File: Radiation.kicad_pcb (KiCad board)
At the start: 4 copper layers, 102 x 125 mm, 114 parts, among them J1 USB4105-GF-A, J2 USB4105-GF-A, J3 AUDIO JACK, J4 MEM2061-01-188-00-A, J5 1x6 header, Q1 AO3400A, Q2 2N7002-TP, Q3 2N7002-TP, Q4 BC846, T1 FL2810-1L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

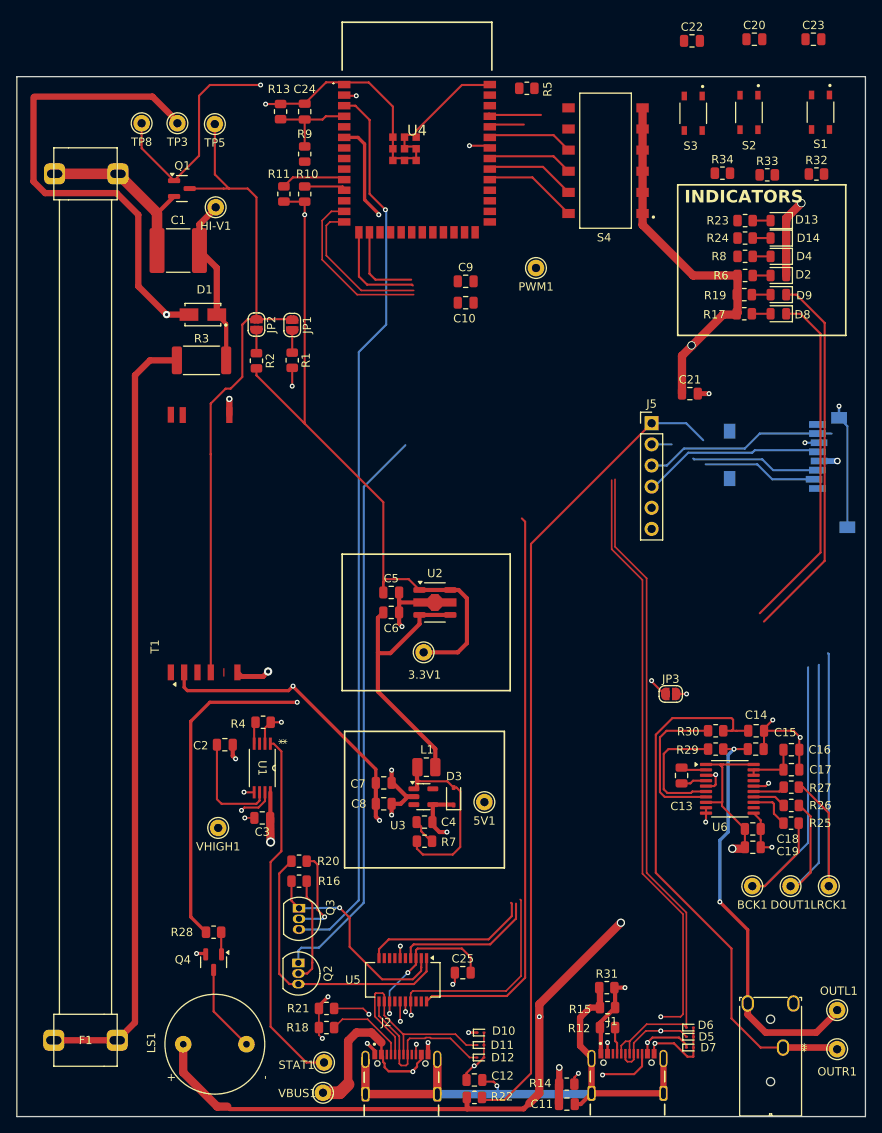
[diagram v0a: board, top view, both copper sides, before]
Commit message: Updated schematics/ pcb
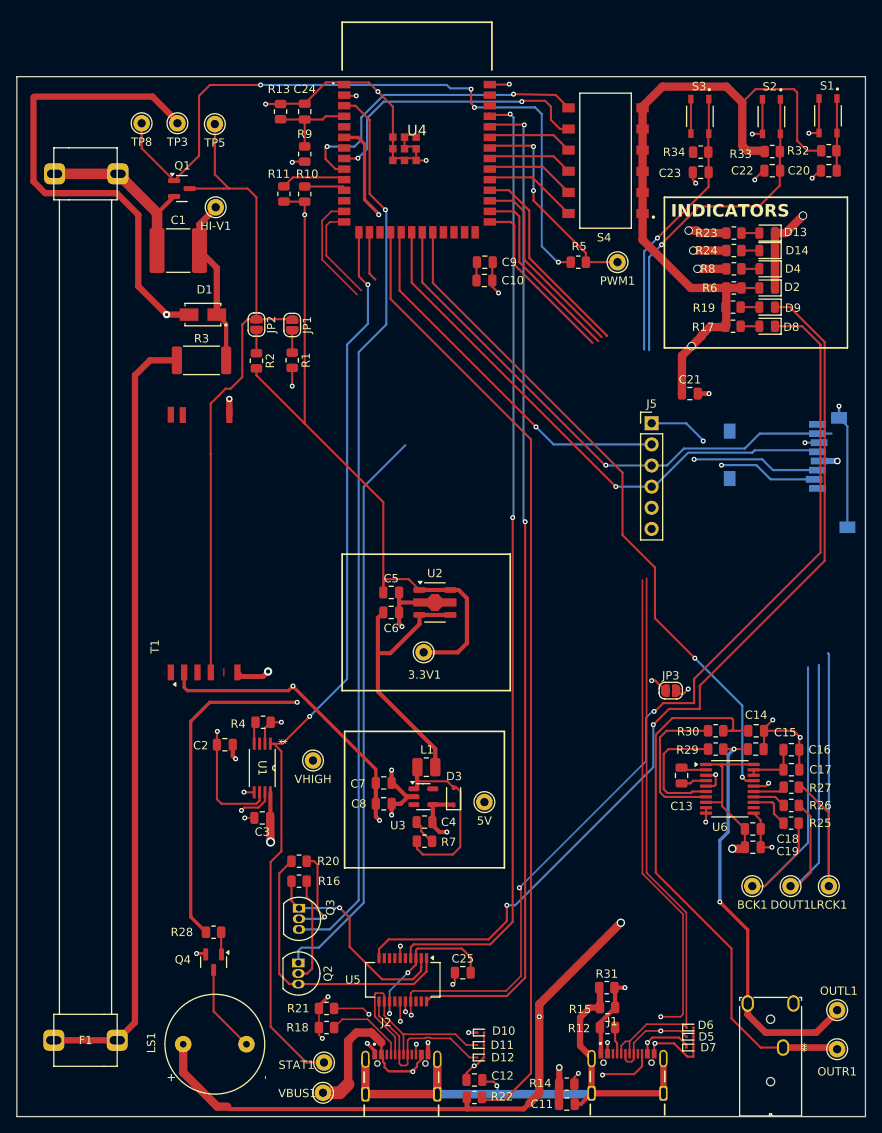
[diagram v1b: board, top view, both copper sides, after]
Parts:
- moved R5 21.8 mm to (104.7, 84.2), turned to 0 degrees
- moved C23 21.0 mm to (119.4, 73.4)
- moved C22 18.3 mm to (128.0, 73.2)
- moved C20 18.2 mm to (134.8, 73.2)
- moved VHIGH 14.0 mm to (72.8, 144.1)
- moved PWM1 9.82 mm to (109.4, 84.2)
- moved R34 3.64 mm to (119.4, 71.0), turned to 180 degrees
- moved C10 3.49 mm to (93.4, 86.4)
- moved C9 3.25 mm to (93.5, 84.2)
- moved R32 3.17 mm to (134.8, 70.8), turned to 180 degrees
- moved R33 2.86 mm to (128.0, 70.9), turned to 180 degrees
- moved S2 2.75 mm to (127.9, 66.7)
- moved D13 2.02 mm to (127.4, 80.7)
- moved D14 2.02 mm to (127.4, 82.8)
- moved D2 2.02 mm to (127.4, 87.3)
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- renumbered 5V1 to 5V, VHIGH1 to VHIGH
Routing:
- net VBUS: track 103.2 -> 213.6 mm, vias 5 -> 6
- net /MCU/TX: track 23.5 -> 115.0 mm, vias 0 -> 2
- net +VBAT: track 13.1 -> 98.0 mm, vias 0 -> 3
- net /MUTE: track 0.00 -> 82.4 mm, vias 0 -> 2
- net +3.3V: track 313.0 -> 377.3 mm
- net GND: track 348.0 -> 409.3 mm, vias 26 -> 35
- net /VSTAT: track 56.1 -> 111.0 mm, vias 0 -> 2
- net /MCU/RX_LED: track 67.8 -> 116.9 mm, vias 1 -> 3
- net /MOSI: track 17.9 -> 66.6 mm, vias 0 -> 2
- net /MCU/TX_LED: track 65.3 -> 113.7 mm, vias 0 -> 2
- net /MCU/RX: track 72.5 -> 119.9 mm, vias 0 -> 2
- net /SCK: track 21.8 -> 67.2 mm, vias 0 -> 1
- net /MISO: track 23.2 -> 65.8 mm, vias 0 -> 1
- net /EN: track 108.1 -> 149.1 mm, vias 1 -> 2
- net Net-(Q1-G): track 45.7 -> 84.9 mm, vias 1 -> 4
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- added copper zone on In2.Cu, net +500V

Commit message: revisions after design review by Ted Yapo
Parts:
- removed 5V, VHIGH: TestPoint, Connector_Pin:Pin_D1.0mm_L10.0mm
- added 5V1: TestPoint, Connector_Pin:Pin_D1.0mm_L10.0mm, F.Cu at (93.5, 148.9)
- added C26: 2.2uF, Capacitor_SMD:C_0805_2012Metric, F.Cu at (118.7, 152.8)
- added VHIGH1: TestPoint, Connector_Pin:Pin_D1.0mm_L10.0mm, F.Cu at (93.4, 131.7)
- moved R27 78.8 mm to (97.9, 75.5), turned to 180 degrees
- moved R26 77.9 mm to (99.8, 77.8), turned to 180 degrees
- moved R25 77.8 mm to (99.9, 80.0), turned to 180 degrees
- moved LRCK1 11.2 mm to (135.3, 148.0)
- moved BCK1 10.3 mm to (135.3, 155.8)
- moved DOUT1 8.77 mm to (135.2, 152.0)
- moved OUTL1 4.70 mm to (135.8, 178.8)
- moved OUTR1 4.70 mm to (135.8, 174.1)
- moved R9 3.10 mm to (68.9, 70.1)
- moved S4 1.23 mm to (108.8, 71.1)
- moved C10 1.13 mm to (93.2, 87.5)
- moved C9 1.13 mm to (93.2, 85.3)
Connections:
- C16 pad 1: Net-(U6-DGND) -> Net-(U6-LDOO)
- C17 pad 1: Net-(U6-DGND) -> Net-(U6-LDOO)
- J3 pad 1: /Audio/OUTR -> AGND
- J3 pad 3: AGND -> /Audio/OUTR
- R25 pad 1: Net-(U6-BCK) -> /I2S_BCK
- R25 pad 2: /I2S_BCK -> Net-(U4-IO35)
- R26 pad 1: Net-(U6-DIN) -> /I2S_LRCK
- R26 pad 2: /I2S_DOUT -> Net-(U4-IO36)
- R27 pad 1: Net-(U6-LRCK) -> /I2S_DOUT
- R27 pad 2: /I2S_LRCK -> Net-(U4-IO37)
- U4 pad 28: /I2S_BCK -> Net-(U4-IO35)
- U4 pad 29: /I2S_LRCK -> Net-(U4-IO36)
- U4 pad 30: /I2S_DOUT -> Net-(U4-IO37)
- U6 pad 12: unconnected-(U6-SCK-Pad12) -> AGND
- U6 pad 13: Net-(U6-BCK) -> /I2S_BCK
- U6 pad 14: Net-(U6-DIN) -> /I2S_DOUT
- U6 pad 15: Net-(U6-LRCK) -> /I2S_LRCK
- U6 pad 18: Net-(U6-DGND) -> Net-(U6-LDOO)
- U6 pad 19: Net-(U6-DGND) -> AGND
- U6 pad 5: AGND -> Net-(U6-VNEG)
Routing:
- net /GPIO0: track 98.6 -> 166.5 mm, vias 0 -> 5
- net +VBAT: track 98.0 -> 160.8 mm, vias 3 -> 5
- net +5V: track 102.0 -> 159.9 mm, vias 5 -> 7
- net Net-(U4-IO35): track 0.00 -> 50.5 mm, vias 0 -> 3
- net /USB_D+: track 82.1 -> 130.9 mm, vias 2 -> 4
- net /USB_D-: track 81.0 -> 129.5 mm
- net +3.3V: track 377.3 -> 425.3 mm, vias 8 -> 13
- net AGND: track 61.3 -> 40.9 mm, vias 7 -> 9
- net /I2S_LRCK: track 65.3 -> 46.1 mm, vias 0 -> 1
- net /I2S_BCK: track 63.5 -> 45.8 mm, vias 0 -> 1
- net /CS: track 138.5 -> 153.8 mm, vias 2 -> 4
- net /GPIO46: track 39.6 -> 28.1 mm
- net /EN: track 149.1 -> 137.9 mm
- net Net-(U6-VNEG): track 0.00 -> 9.84 mm
- net /I2S_DOUT: track 64.8 -> 55.5 mm, vias 0 -> 1
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- added copper zone on In2.Cu, net +3.3V
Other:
- board text removed: "MFS V. PROTO1 FEBRUARY 1, 2025"
